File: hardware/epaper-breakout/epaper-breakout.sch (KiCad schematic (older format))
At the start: 89 parts, among them J1 XF2M-3315-1A, J2 C10418, J3 Conn_02x06_Counter_Clockwise, J4 ED060SC4, J5 Conn_01x02_Male, Q1 AO3401A, Q2 AO3401A, Q3 MMBT3904, Q4 MMBT3904, Q5 AO3401A, Q6 MMBT3904, U1 MCP1700-3302E_SOT23, U10 ED060SC7, U11 TP4056, U12 CH340C, U2 LT1945, U3 LT1945, U4 XC6206PxxxMR, U5 ESP32-WROVER, U6 ED060XC5, U7 LM358, U8 74HC4094-normal, U9 MCP9700AT-ETT

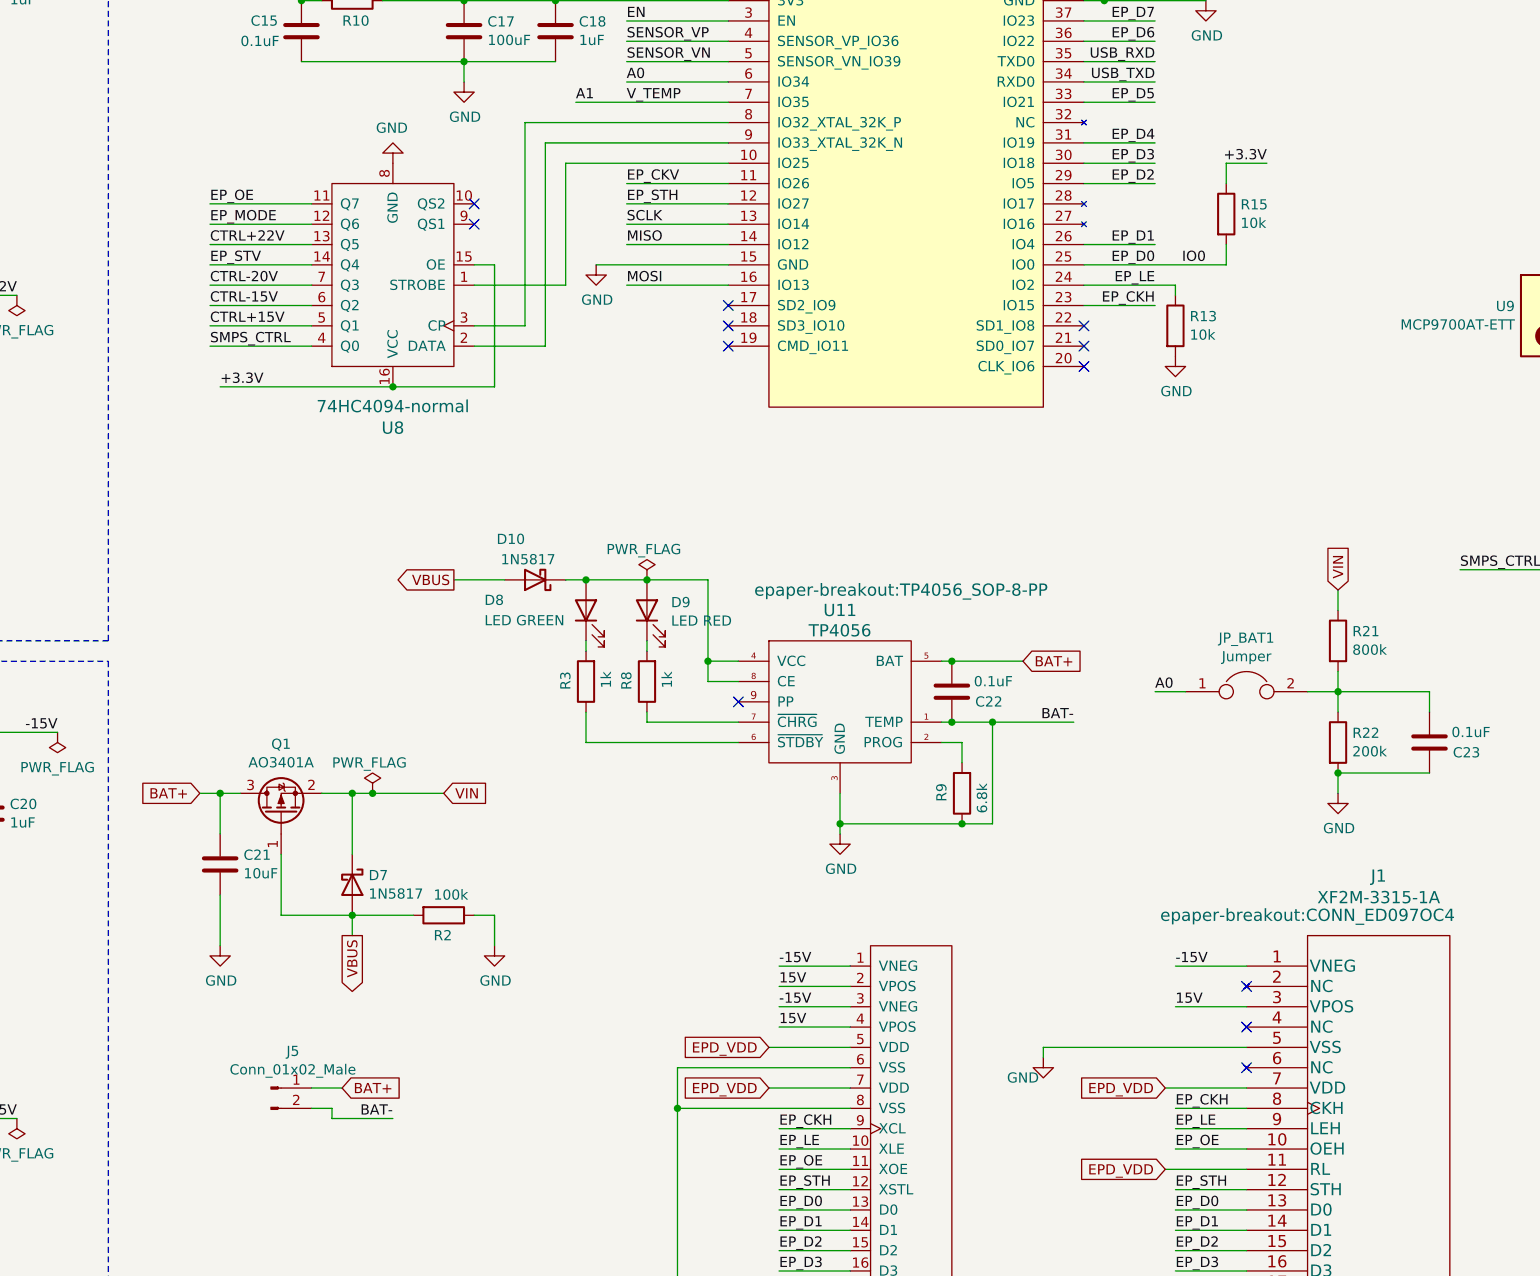
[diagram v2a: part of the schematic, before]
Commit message: v5: swap gpio 0 and 19
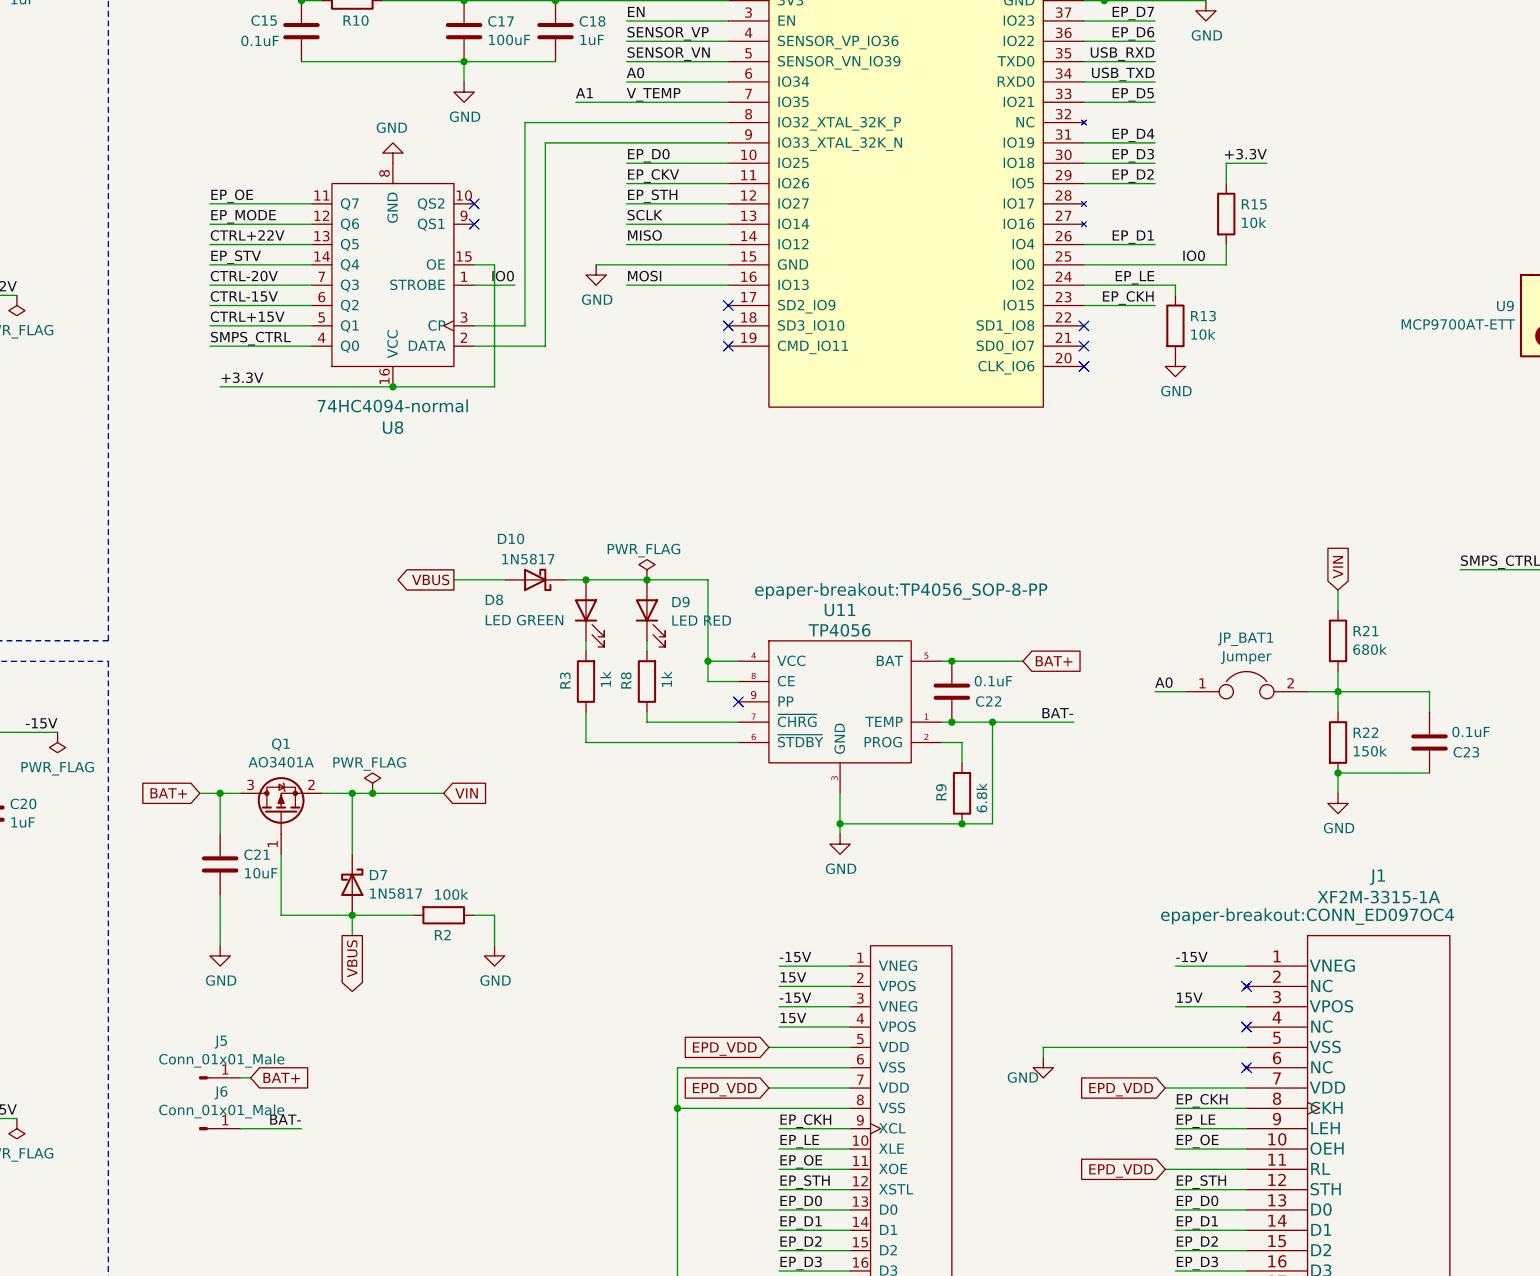
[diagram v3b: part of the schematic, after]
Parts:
- removed J5: Conn_01x02_Male, Connector_PinHeader_2.54mm:PinHeader_1x02_P2.54mm_Vertical, symbol Connector:Conn_01x02_Male
- added J5, J6: Conn_01x01_Male, Connector_PinHeader_2.54mm:PinHeader_1x01_P2.54mm_Vertical, symbol Connector:Conn_01x01_Male
- R21: value 800k -> 680k; LCSC (none) -> C17797
- R22: value 200k -> 150k; LCSC (none) -> C17797
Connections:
- net BAT+: now also J5.1 (Pin_1)
- net EP_D0: now also U5.10 (IO25); no longer Q4.3 (C), R15.2, U5.25 (IO0)
- net GND: now also J6.1 (Pin_1)
- net IO0: now reaches U8.1 (STROBE)
- net IO0: now also Q4.3 (C), R15.2, U5.25 (IO0); no longer U5.10 (IO25)
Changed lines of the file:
@@
 Text Label 7500 2300 0    50   ~ 0
 EP_CKV
-Text Label 10100 2700 2    50   ~ 0
+Text Label 7500 2200 0    50   ~ 0
 EP_D0
 Text Label 10100 2300 2    50   ~ 0
@@
 	7100 2100 7100 3100
 Wire Wire Line
-	6750 2800 7200 2800
-Wire Wire Line
-	7200 2800 7200 2200
-Wire Wire Line
-	7200 2200 8000 2200
-Wire Wire Line
 	10100 2100 9750 2100
 Wire Wire Line
@@
 Wire Wire Line
 	7600 4250 7900 4250
-$Comp
-L Connector:Conn_01x02_Male J5
-U 1 1 655CB8A7
-P 5750 6750
-F 0 "J5" H 5858 6931 50  0000 C CNN
-F 1 "Conn_01x02_Male" H 5858 6840 50  0000 C CNN
-F 2 "Connector_PinHeader_2.54mm:PinHeader_1x02_P2.54mm_Vertical" H 5750 6750 50  0001 C CNN
-F 3 "~" H 5750 6750 50  0001 C CNN
-	1    5750 6750
-	1    0    0    -1
-$EndComp
-Text GLabel 6100 6750 2    50   Input ~ 0
+Text GLabel 5650 6700 2    50   Input ~ 0
 BAT+
-Wire Wire Line
-	5950 6750 6100 6750
 Text GLabel 12600 1700 0    50   Input ~ 0
 VBUS
@@
 P 11000 5050
 F 0 "R22" H 11070 5096 50  0000 L CNN
-F 1 "200k" H 11070 5005 50  0000 L CNN
+F 1 "150k" H 11070 5005 50  0000 L CNN
 F 2 "Resistor_SMD:R_0805_2012Metric" V 10930 5050 50  0001 C CNN
 F 3 "~" H 11000 5050 50  0001 C CNN
+F 4 " C17797" H 11000 5050 50  0001 C CNN "LCSC"
 	1    11000 5050
 	1    0    0    -1
@@
 P 11000 4550
 F 0 "R21" H 11070 4596 50  0000 L CNN
-F 1 "800k" H 11070 4505 50  0000 L CNN
+F 1 "680k" H 11070 4505 50  0000 L CNN
 F 2 "Resistor_SMD:R_0805_2012Metric" V 10930 4550 50  0001 C CNN
 F 3 "~" H 11000 4550 50  0001 C CNN
+F 4 " C17797" H 11000 4550 50  0001 C CNN "LCSC"
 	1    11000 4550
 	1    0    0    -1
@@
 Wire Wire Line
 	9300 4950 9700 4950
-Text Label 6350 6900 2    50   ~ 0
+Text Label 5900 6950 2    50   ~ 0
 BAT-
 Wire Wire Line
-	5950 6850 6050 6850
-Wire Wire Line
-	6050 6850 6050 6900
-Wire Wire Line
-	6050 6900 6350 6900
+	5600 6950 5900 6950
 $Comp
 L power:PWR_FLAG #FLG0103
@@
 	11450 5200 11000 5200
 Connection ~ 11000 5200
+Text Label 6950 2800 2    50   ~ 0
+IO0
+Wire Wire Line
+	8000 2200 7500 2200
+Wire Wire Line
+	6750 2800 6950 2800
+$Comp
+L Connector:Conn_01x01_Male J5
+U 1 1 6016D7FE
+P 5400 6700
+F 0 "J5" H 5508 6881 50  0000 C CNN
+F 1 "Conn_01x01_Male" H 5508 6790 50  0000 C CNN
+F 2 "Connector_PinHeader_2.54mm:PinHeader_1x01_P2.54mm_Vertical" H 5400 6700 50  0001 C CNN
+F 3 "~" H 5400 6700 50  0001 C CNN
+	1    5400 6700
+	1    0    0    -1
+$EndComp
+$Comp
+L Connector:Conn_01x01_Male J6
+U 1 1 6016F621
+P 5400 6950
+F 0 "J6" H 5508 7131 50  0000 C CNN
+F 1 "Conn_01x01_Male" H 5508 7040 50  0000 C CNN
+F 2 "Connector_PinHeader_2.54mm:PinHeader_1x01_P2.54mm_Vertical" H 5400 6950 50  0001 C CNN
+F 3 "~" H 5400 6950 50  0001 C CNN
+	1    5400 6950
+	1    0    0    -1
+$EndComp
+Wire Wire Line
+	5650 6700 5600 6700
 $EndSCHEMATC

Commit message: v5 prototype
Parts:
- D8: LCSC (none) -> C2297
- D9: LCSC (none) -> C84256
- R12: LCSC C17414 -> C17513
- R22: LCSC C17797 -> C17470
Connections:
- net EPD_VDD: now also U9.1 (Vdd)
- net VIN: no longer U9.1 (Vdd)
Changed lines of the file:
@@
 F 2 "Resistor_SMD:R_0805_2012Metric" V 12130 4200 50  0001 C CNN
 F 3 "~" H 12200 4200 50  0001 C CNN
-F 4 "C17414" H 12200 4200 50  0001 C CNN "LCSC"
+F 4 "C17513" H 12200 4200 50  0001 C CNN "LCSC"
 	1    12200 4200
 	0    1    1    0
@@
 F 2 "LED_SMD:LED_0805_2012Metric" H 7600 4400 50  0001 C CNN
 F 3 "~" H 7600 4400 50  0001 C CNN
+F 4 " C84256" V 7600 4400 50  0001 C CNN "LCSC"
 	1    7600 4400
 	0    -1   -1   0
@@
 F 2 "LED_SMD:LED_0805_2012Metric" H 7300 4400 50  0001 C CNN
 F 3 "~" H 7300 4400 50  0001 C CNN
+F 4 "C2297" V 7300 4400 50  0001 C CNN "LCSC"
 	1    7300 4400
 	0    -1   -1   0
@@
 Wire Wire Line
 	1850 10600 1750 10600
-Text GLabel 12200 2350 2    50   Input ~ 0
-VIN
 $Comp
 L Device:Jumper JP_TEMP1
@@
 F 2 "Resistor_SMD:R_0805_2012Metric" V 10930 5050 50  0001 C CNN
 F 3 "~" H 11000 5050 50  0001 C CNN
-F 4 " C17797" H 11000 5050 50  0001 C CNN "LCSC"
+F 4 " C17470" H 11000 5050 50  0001 C CNN "LCSC"
 	1    11000 5050
 	1    0    0    -1
@@
 Wire Wire Line
 	5650 6700 5600 6700
+Text GLabel 12200 2350 1    50   Input ~ 0
+EPD_VDD
 $EndSCHEMATC

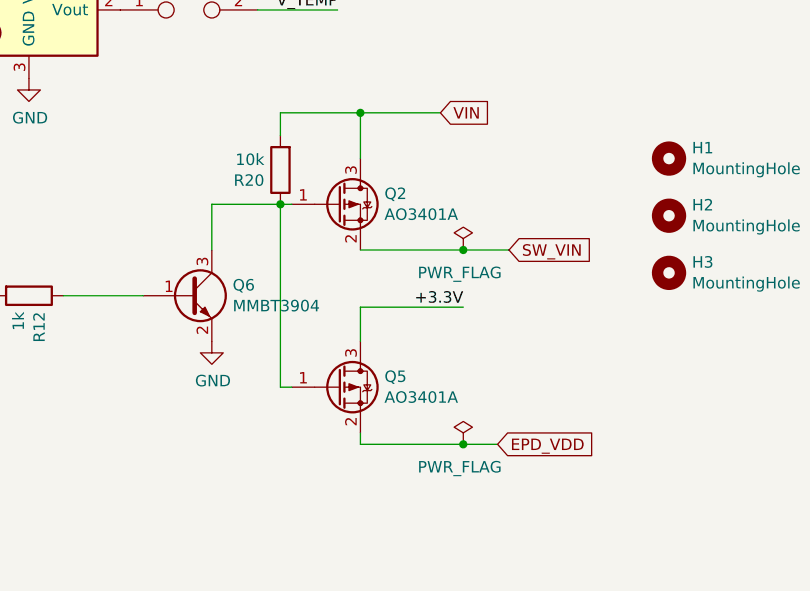
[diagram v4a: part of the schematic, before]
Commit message: v5: fix mosfet orientation
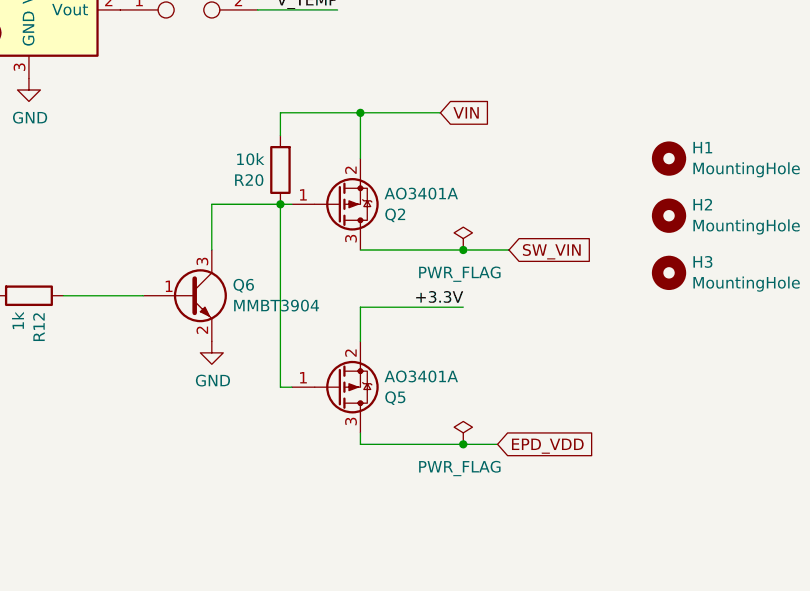
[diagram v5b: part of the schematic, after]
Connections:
- net +3.3V: now also Q5.2 (S); no longer Q5.3 (D)
- net EPD_VDD: now also Q5.3 (D); no longer Q5.2 (S)
- net SW_VIN: now also Q2.3 (D); no longer Q2.2 (S)
- net VIN: now also Q2.2 (S); no longer Q2.3 (D)
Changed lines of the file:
@@
 F 4 " C15127" H 13550 3800 50  0001 C CNN "LCSC"
 	1    13550 3800
-	1    0    0    -1
+	1    0    0    1
 $EndComp
 $Comp
@@
 F 4 " C15127" H 13550 4600 50  0001 C CNN "LCSC"
 	1    13550 4600
-	1    0    0    -1
+	1    0    0    1
 $EndComp
 Text GLabel 14250 4850 2    50   Input ~ 0
